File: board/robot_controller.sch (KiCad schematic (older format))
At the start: 57 parts, among them U2 STM32F405-144

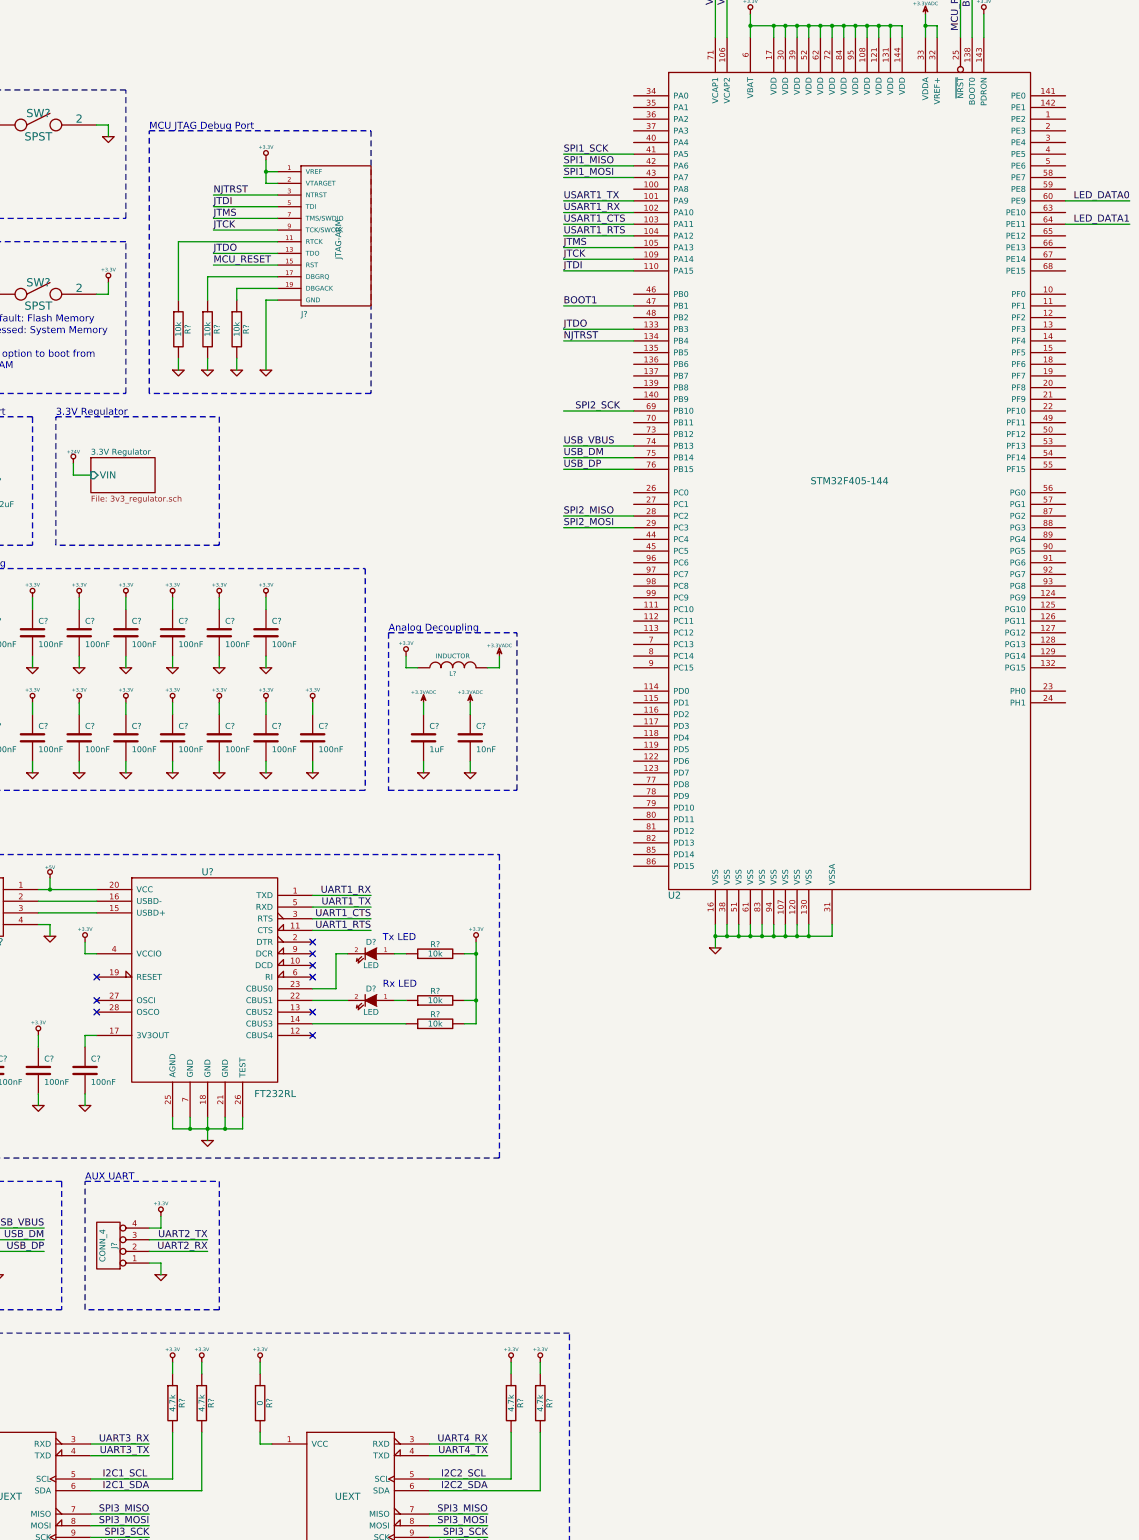
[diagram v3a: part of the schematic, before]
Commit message: Connected the UEXT UARTS/I2C/SPI in the right places
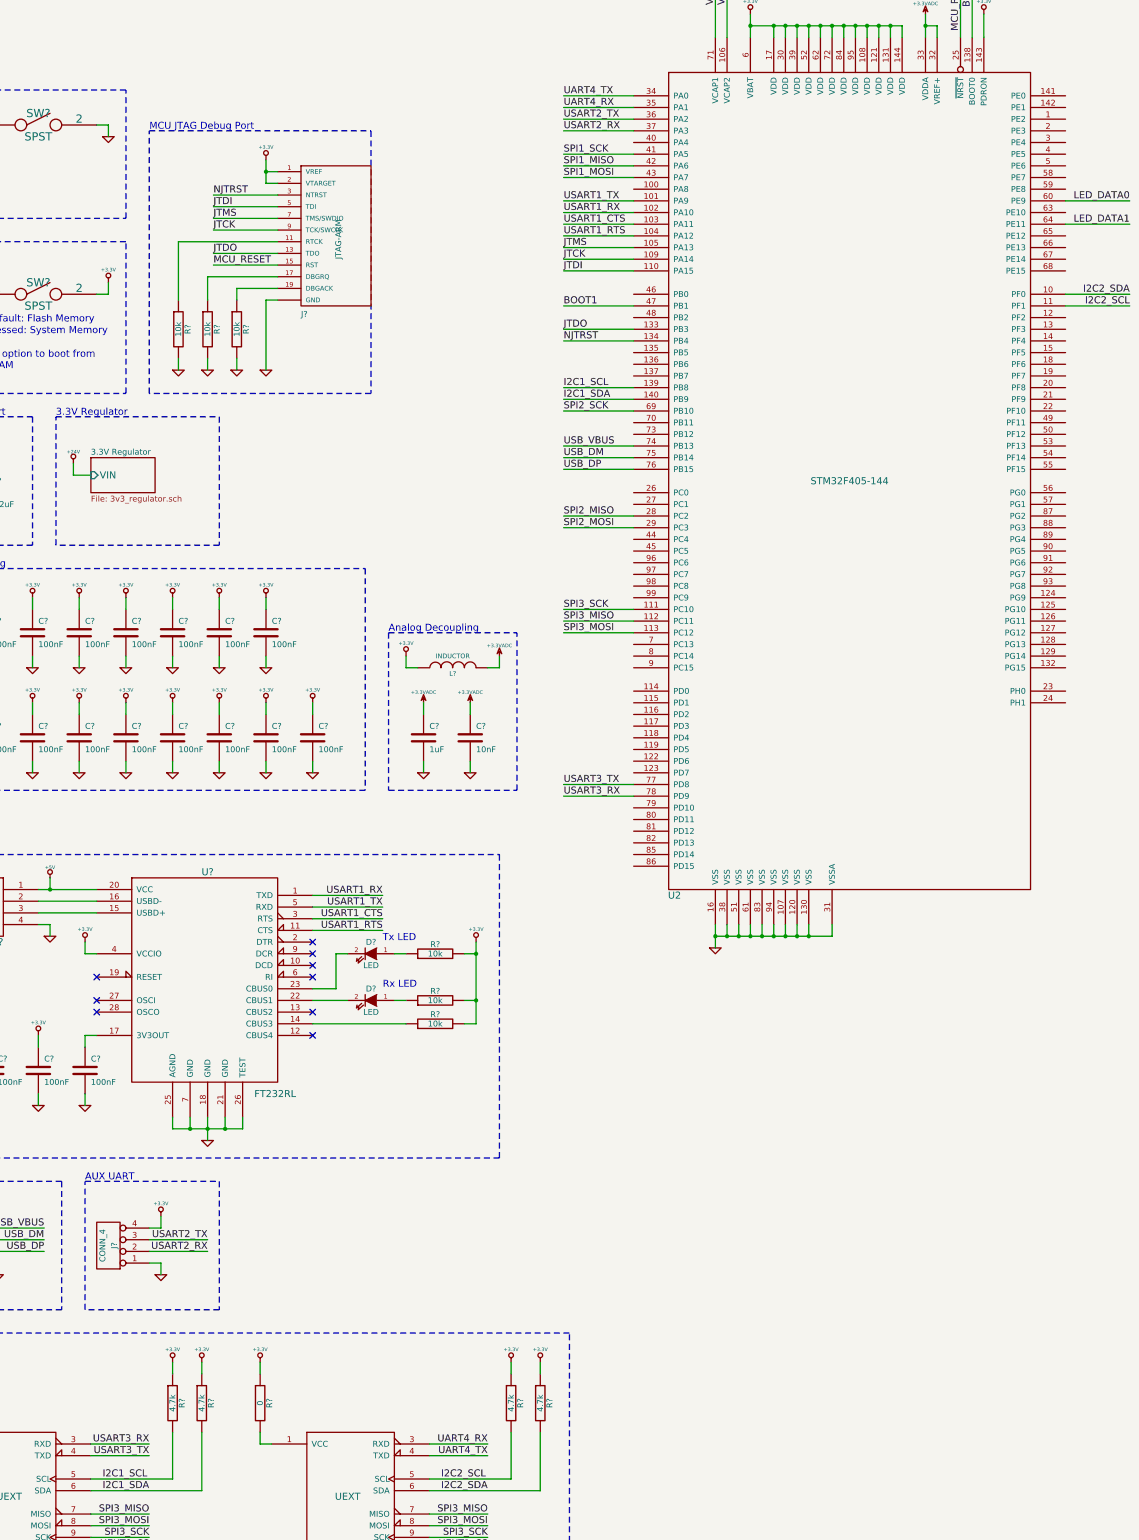
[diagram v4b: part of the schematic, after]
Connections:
- net UART1_CTS is gone; now on net USART1_CTS: U?.3 (RTS)
- net UART1_RTS is gone; now on net USART1_RTS: U?.11 (CTS)
- net UART1_RX is gone; now on net USART1_RX: U?.1 (TXD)
- net UART1_TX is gone; now on net USART1_TX: U?.5 (RXD)
- net UART2_RX is gone; now on net USART2_RX: J?.2 (P2)
- net UART2_TX is gone; now on net USART2_TX: J?.3 (P3)
- net UART3_RX is gone; now on net USART3_RX: UEXT0.3 (RXD)
- net UART3_TX is gone; now on net USART3_TX: UEXT0.4 (TXD)
- net I2C1_SCL: now also U2.139 (PB8)
- net I2C1_SDA: now also U2.140 (PB9)
- net I2C2_SCL: now also U2.11 (PF1)
- net I2C2_SDA: now also U2.10 (PF0)
- net SPI3_MISO: now also U2.112 (PC11)
- net SPI3_MOSI: now also U2.113 (PC12)
- net SPI3_SCK: now also U2.111 (PC10)
- net UART4_RX: now also U2.35 (PA1)
- net UART4_TX: now also U2.34 (PA0)
- net USART2_TX: now reaches U2.36 (PA2)
- net USART2_RX: now reaches U2.37 (PA3)
- net USART3_TX: now reaches U2.77 (PD8)
- net USART3_RX: now reaches U2.78 (PD9)
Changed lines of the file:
@@
 	0    -1   -1   0
 $EndComp
-Text Label 33750 20700 2    60   ~ 0
-UART1_RX
-Text Label 33750 20800 2    60   ~ 0
-UART1_TX
-Text Label 33750 20900 2    60   ~ 0
-UART1_CTS
-Text Label 33750 21000 2    60   ~ 0
-UART1_RTS
+Text Label 33850 20700 2    60   ~ 0
+USART1_RX
+Text Label 33850 20800 2    60   ~ 0
+USART1_TX
+Text Label 33850 20900 2    60   ~ 0
+USART1_CTS
+Text Label 33850 21000 2    60   ~ 0
+USART1_RTS
 $Comp
 L GND #PWR?
@@
 Text Label 35400 17450 0    60   ~ 0
 SPI2_MISO
-Text Label 35500 16550 0    60   ~ 0
+Text Label 35400 16550 0    60   ~ 0
 SPI2_SCK
 Text Notes 19000 15000 0    60   ~ 0
@@
 $EndComp
 Text Label 32350 23750 2    60   ~ 0
-UART2_RX
+USART2_RX
 Text Label 32350 23650 2    60   ~ 0
-UART2_TX
+USART2_TX
 Text Notes 31300 23150 0    60   ~ 0
 AUX UART
 Text Label 31850 25400 2    60   ~ 0
-UART3_RX
+USART3_RX
 Text Label 31850 25500 2    60   ~ 0
-UART3_TX
+USART3_TX
 $Comp
 L R R?
@@
 NoConn ~ 20250 20400
 NoConn ~ 23500 19150
+$Comp
+L +3.3VADC #PWR?
+U 1 1 52F401B1
+P 38500 13150
+F 0 "#PWR?" H 38500 13270 20  0001 C CNN
+F 1 "+3.3VADC" H 38500 13240 30  0000 C CNN
+F 2 "" H 38500 13150 60  0000 C CNN
+F 3 "" H 38500 13150 60  0000 C CNN
+	1    38500 13150
+	1    0    0    -1
+$EndComp
+$Comp
+L +3.3VADC #PWR?
+U 1 1 52F42BD5
+P 34200 19050
+F 0 "#PWR?" H 34200 19170 20  0001 C CNN
+F 1 "+3.3VADC" H 34200 19140 30  0000 C CNN
+F 2 "" H 34200 19050 60  0000 C CNN
+F 3 "" H 34200 19050 60  0000 C CNN
+	1    34200 19050
+	1    0    0    -1
+$EndComp
+$Comp
+L +3.3VADC #PWR?
+U 1 1 52F436A2
+P 34600 19050
+F 0 "#PWR?" H 34600 19170 20  0001 C CNN
+F 1 "+3.3VADC" H 34600 19140 30  0000 C CNN
+F 2 "" H 34600 19050 60  0000 C CNN
+F 3 "" H 34600 19050 60  0000 C CNN
+	1    34600 19050
+	1    0    0    -1
+$EndComp
+$Comp
+L +3.3VADC #PWR?
+U 1 1 52F45651
+P 34850 18650
+F 0 "#PWR?" H 34850 18770 20  0001 C CNN
+F 1 "+3.3VADC" H 34850 18740 30  0000 C CNN
+F 2 "" H 34850 18650 60  0000 C CNN
+F 3 "" H 34850 18650 60  0000 C CNN
+	1    34850 18650
+	1    0    0    -1
+$EndComp
+$Comp
+L +3.3V #PWR?
+U 1 1 52F4565C
+P 34050 18650
+F 0 "#PWR?" H 34050 18610 30  0001 C CNN
+F 1 "+3.3V" H 34050 18760 30  0000 C CNN
+F 2 "" H 34050 18650 60  0000 C CNN
+F 3 "" H 34050 18650 60  0000 C CNN
+	1    34050 18650
+	1    0    0    -1
+$EndComp
+$Comp
+L INDUCTOR L?
+U 1 1 52F4570B
+P 34450 18750
+F 0 "L?" V 34400 18750 40  0000 C CNN
+F 1 "INDUCTOR" V 34550 18750 40  0000 C CNN
+F 2 "" H 34450 18750 60  0000 C CNN
+F 3 "" H 34450 18750 60  0000 C CNN
+	1    34450 18750
+	0    -1   -1   0
+$EndComp
+Text Notes 31050 16600 0    60   ~ 0
+3.3V Regulator
+$Comp
+L CONN_2 P?
+U 1 1 52F70171
+P 25250 15800
+F 0 "P?" V 25200 15800 40  0000 C CNN
+F 1 "CONN_2" V 25300 15800 40  0000 C CNN
+F 2 "" H 25250 15800 60  0000 C CNN
+F 3 "" H 25250 15800 60  0000 C CNN
+	1    25250 15800
+	-1   0    0    -1
+$EndComp
+$Comp
+L GND #PWR?
+U 1 1 52F70A93
+P 25700 16000
+F 0 "#PWR?" H 25700 16000 30  0001 C CNN
+F 1 "GND" H 25700 15930 30  0001 C CNN
+F 2 "" H 25700 16000 60  0000 C CNN
+F 3 "" H 25700 16000 60  0000 C CNN
+	1    25700 16000
+	1    0    0    -1
+$EndComp
+$Comp
+L +24V #PWR?
+U 1 1 52F75202
+P 31200 17000
+F 0 "#PWR?" H 31200 16950 20  0001 C CNN
+F 1 "+24V" H 31200 17100 30  0000 C CNN
+F 2 "" H 31200 17000 60  0000 C CNN
+F 3 "" H 31200 17000 60  0000 C CNN
+	1    31200 17000
+	1    0    0    -1
+$EndComp
+$Comp
+L +24V #PWR?
+U 1 1 52F76574
+P 25700 15600
+F 0 "#PWR?" H 25700 15550 20  0001 C CNN
+F 1 "+24V" H 25700 15700 30  0000 C CNN
+F 2 "" H 25700 15600 60  0000 C CNN
+F 3 "" H 25700 15600 60  0000 C CNN
+	1    25700 15600
+	1    0    0    -1
+$EndComp
+Text Notes 25400 19400 0    60   ~ 0
+Ideally the voltage at\n24V_ADC should be very\nclose to: 0.5 * 3.3V
+Text Label 35400 16850 0    60   ~ 0
+USB_VBUS
+Text Label 30950 23550 2    60   ~ 0
+USB_VBUS
+Text Label 35400 18450 0    60   ~ 0
+SPI3_MOSI
+Text Label 35400 18350 0    60   ~ 0
+SPI3_MISO
+Text Label 35400 18250 0    60   ~ 0
+SPI3_SCK
+Text Label 35400 16350 0    60   ~ 0
+I2C1_SCL
+Text Label 35400 16450 0    60   ~ 0
+I2C1_SDA
+Text Label 40250 15550 2    60   ~ 0
+I2C2_SDA
+Text Label 40250 15650 2    60   ~ 0
+I2C2_SCL
+Text Label 35400 13850 0    60   ~ 0
+UART4_TX
+Text Label 35400 13950 0    60   ~ 0
+UART4_RX
+Text Label 35400 14050 0    60   ~ 0
+USART2_TX
+Text Label 35400 14150 0    60   ~ 0
+USART2_RX
+Text Label 35400 19750 0    60   ~ 0
+USART3_TX
+Text Label 35400 19850 0    60   ~ 0
+USART3_RX
 Wire Wire Line
 	38800 12800 38800 13350
@@
 	34650 21100 34650 21800
 Wire Wire Line
-	33250 20900 33750 20900
-Wire Wire Line
-	33250 21000 33750 21000
-Wire Wire Line
-	33250 20800 33750 20800
-Wire Wire Line
-	33250 20700 33750 20700
+	33250 20900 33850 20900
+Wire Wire Line
+	33250 21000 33850 21000
+Wire Wire Line
+	33250 20800 33850 20800
+Wire Wire Line
+	33250 20700 33850 20700
 Wire Wire Line
 	30900 22400 30900 22500
@@
 Wire Notes Line
 	35450 24450 29650 24450
-$Comp
-L +3.3VADC #PWR?
-U 1 1 52F401B1
-P 38500 13150
-F 0 "#PWR?" H 38500 13270 20  0001 C CNN
-F 1 "+3.3VADC" H 38500 13240 30  0000 C CNN
-F 2 "" H 38500 13150 60  0000 C CNN
-F 3 "" H 38500 13150 60  0000 C CNN
-	1    38500 13150
-	1    0    0    -1
-$EndComp
 Wire Wire Line
 	37000 13250 38300 13250
 Wire Wire Line
 	38500 13250 38600 13250
-$Comp
-L +3.3VADC #PWR?
-U 1 1 52F42BD5
-P 34200 19050
-F 0 "#PWR?" H 34200 19170 20  0001 C CNN
-F 1 "+3.3VADC" H 34200 19140 30  0000 C CNN
-F 2 "" H 34200 19050 60  0000 C CNN
-F 3 "" H 34200 19050 60  0000 C CNN
-	1    34200 19050
-	1    0    0    -1
-$EndComp
-$Comp
-L +3.3VADC #PWR?
-U 1 1 52F436A2
-P 34600 19050
-F 0 "#PWR?" H 34600 19170 20  0001 C CNN
-F 1 "+3.3VADC" H 34600 19140 30  0000 C CNN
-F 2 "" H 34600 19050 60  0000 C CNN
-F 3 "" H 34600 19050 60  0000 C CNN
-	1    34600 19050
-	1    0    0    -1
-$EndComp
-$Comp
-L +3.3VADC #PWR?
-U 1 1 52F45651
-P 34850 18650
-F 0 "#PWR?" H 34850 18770 20  0001 C CNN
-F 1 "+3.3VADC" H 34850 18740 30  0000 C CNN
-F 2 "" H 34850 18650 60  0000 C CNN
-F 3 "" H 34850 18650 60  0000 C CNN
-	1    34850 18650
-	1    0    0    -1
-$EndComp
-$Comp
-L +3.3V #PWR?
-U 1 1 52F4565C
-P 34050 18650
-F 0 "#PWR?" H 34050 18610 30  0001 C CNN
-F 1 "+3.3V" H 34050 18760 30  0000 C CNN
-F 2 "" H 34050 18650 60  0000 C CNN
-F 3 "" H 34050 18650 60  0000 C CNN
-	1    34050 18650
-	1    0    0    -1
-$EndComp
-$Comp
-L INDUCTOR L?
-U 1 1 52F4570B
-P 34450 18750
-F 0 "L?" V 34400 18750 40  0000 C CNN
-F 1 "INDUCTOR" V 34550 18750 40  0000 C CNN
-F 2 "" H 34450 18750 60  0000 C CNN
-F 3 "" H 34450 18750 60  0000 C CNN
-	1    34450 18750
-	0    -1   -1   0
-$EndComp
 Wire Wire Line
 	34050 18650 34050 18750
@@
 Wire Wire Line
 	31200 17100 31350 17100
-Text Notes 31050 16600 0    60   ~ 0
-3.3V Regulator
 Wire Notes Line
 	31050 16600 32450 16600
@@
 Wire Notes Line
 	31050 17700 31050 16600
-$Comp
-L CONN_2 P?
-U 1 1 52F70171
-P 25250 15800
-F 0 "P?" V 25200 15800 40  0000 C CNN
-F 1 "CONN_2" V 25300 15800 40  0000 C CNN
-F 2 "" H 25250 15800 60  0000 C CNN
-F 3 "" H 25250 15800 60  0000 C CNN
-	1    25250 15800
-	-1   0    0    -1
-$EndComp
-$Comp
-L GND #PWR?
-U 1 1 52F70A93
-P 25700 16000
-F 0 "#PWR?" H 25700 16000 30  0001 C CNN
-F 1 "GND" H 25700 15930 30  0001 C CNN
-F 2 "" H 25700 16000 60  0000 C CNN
-F 3 "" H 25700 16000 60  0000 C CNN
-	1    25700 16000
-	1    0    0    -1
-$EndComp
 Wire Wire Line
 	25700 15600 25700 15700
@@
 Wire Wire Line
 	25700 15900 25700 16000
-$Comp
-L +24V #PWR?
-U 1 1 52F75202
-P 31200 17000
-F 0 "#PWR?" H 31200 16950 20  0001 C CNN
-F 1 "+24V" H 31200 17100 30  0000 C CNN
-F 2 "" H 31200 17000 60  0000 C CNN
-F 3 "" H 31200 17000 60  0000 C CNN
-	1    31200 17000
-	1    0    0    -1
-$EndComp
-$Comp
-L +24V #PWR?
-U 1 1 52F76574
-P 25700 15600
-F 0 "#PWR?" H 25700 15550 20  0001 C CNN
-F 1 "+24V" H 25700 15700 30  0000 C CNN
-F 2 "" H 25700 15600 60  0000 C CNN
-F 3 "" H 25700 15600 60  0000 C CNN
-	1    25700 15600
-	1    0    0    -1
-$EndComp
-Text Notes 25400 19400 0    60   ~ 0
-Ideally the voltage at\n24V_ADC should be very\nclose to: 0.5 * 3.3V
 Wire Wire Line
 	35400 16550 36000 16550
 Wire Wire Line
 	35400 16850 36000 16850
-Text Label 35400 16850 0    60   ~ 0
-USB_VBUS
 Wire Wire Line
 	30450 23550 30950 23550
-Text Label 30950 23550 2    60   ~ 0
-USB_VBUS
+Wire Wire Line
+	35400 18450 36000 18450
+Wire Wire Line
+	35400 18350 36000 18350
+Wire Wire Line
+	35400 18250 36000 18250
+Wire Wire Line
+	35400 16350 36000 16350
+Wire Wire Line
+	35400 16450 36000 16450
+Wire Wire Line
+	39700 15550 40250 15550
+Wire Wire Line
+	40250 15650 39700 15650
+Wire Wire Line
+	36000 13850 35400 13850
+Wire Wire Line
+	35400 13950 36000 13950
+Wire Wire Line
+	35400 14050 36000 14050
+Wire Wire Line
+	35400 14150 36000 14150
+Wire Wire Line
+	36000 19750 35400 19750
+Wire Wire Line
+	35400 19850 36000 19850
 $EndSCHEMATC
